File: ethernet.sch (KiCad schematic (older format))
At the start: 37 parts, among them J2 08B0-1X1T-36-F, U6 DP83848JSQ_NOPB, Y1 ABM8G-25.000MHZ-18-D2Y-T

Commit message: Clean FTDI
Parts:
- removed C117, C118, C119, C129: C_100n_0402_6V3, lpddr4-test-board-footprints:0402-cap, symbol lpddr4-test-board:C_100n_0402_6V3
- removed C127: C_1u_0402, lpddr4-test-board-footprints:0402-cap, symbol lpddr4-test-board:C_1u_0402
- removed R81: R_0R_0402, lpddr4-test-board-footprints:0402-res, symbol lpddr4-test-board:R_0R_0402
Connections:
- net at U6.27 (X2): now also C132.1, Y1.1
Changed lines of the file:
@@
-$EndComp
-$Comp
-L lpddr4-test-board:C_1u_0402 C127
-U 1 1 5F9F438B
-P 12025 4100
-F 0 "C127" H 12050 4200 60  0000 L CNN
-F 1 "C_1u_0402" H 12025 3950 60  0001 C CNN
-F 2 "lpddr4-test-board-footprints:0402-cap" H 12225 4300 60  0001 L CNN
-F 3 "" H 12025 4100 50  0001 C CNN
-F 4 "TDK" H 12225 4500 60  0001 L CNN "Manufacturer"
-F 5 "C1005X6S1A105K050BC" H 12225 4400 60  0001 L CNN "MPN"
-F 6 "1u" H 12050 4000 50  0000 L CNN "Val"
-	1    12025 4100
-	1    0    0    -1
-$EndComp
-$Comp
-L lpddr4-test-board:C_100n_0402_6V3 C129
-U 1 1 5F9F4394
-P 12325 4100
-F 0 "C129" H 12350 4200 60  0000 L CNN
-F 1 "C_100n_0402_6V3" H 12325 3950 60  0001 C CNN
-F 2 "lpddr4-test-board-footprints:0402-cap" H 12525 4300 60  0001 L CNN
-F 3 "" H 12325 4100 50  0001 C CNN
-F 4 "Walsin" H 12525 4500 60  0001 L CNN "Manufacturer"
-F 5 "0402X104K6R3CT" H 12525 4400 60  0001 L CNN "MPN"
-F 6 "100n" H 12350 4000 50  0000 L CNN "Val"
-	1    12325 4100
-	1    0    0    -1
 $EndComp
 $Comp
@@
 Text GLabel 11200 7000 2    50   Input ~ 0
 ETH_MDC
-$Comp
-L lpddr4-test-board:R_0R_0402 R81
-U 1 1 5FABAF2E
-P 11225 6700
-F 0 "R81" H 11025 6750 60  0000 C CNN
-F 1 "R_0R_0402" H 11225 6550 60  0001 C CNN
-F 2 "lpddr4-test-board-footprints:0402-res" H 11425 6900 60  0001 L CNN
-F 3 "" H 11225 6700 50  0001 C CNN
-F 4 "PANASONIC" H 11425 7100 60  0001 L CNN "Manufacturer"
-F 5 "ERJ2GE0R00X" H 11425 7000 60  0001 L CNN "MPN"
-F 6 "0R" H 11400 6650 50  0000 C CNN "Val"
-	1    11225 6700
-	1    0    0    -1
-$EndComp
-Wire Wire Line
-	10875 6700 11075 6700
-Wire Wire Line
-	11375 6700 13275 6700
 Wire Wire Line
 	13275 6700 13275 6850
@@
 Wire Wire Line
 	4500 5350 4300 5350
-$Comp
-L lpddr4-test-board:C_100n_0402_6V3 C117
-U 1 1 5FAAC848
-P 2925 4225
-F 0 "C117" H 2950 4325 60  0000 L CNN
-F 1 "C_100n_0402_6V3" H 2925 4075 60  0001 C CNN
-F 2 "lpddr4-test-board-footprints:0402-cap" H 3125 4425 60  0001 L CNN
-F 3 "" H 2925 4225 50  0001 C CNN
-F 4 "Walsin" H 3125 4625 60  0001 L CNN "Manufacturer"
-F 5 "0402X104K6R3CT" H 3125 4525 60  0001 L CNN "MPN"
-F 6 "100n" H 2950 4125 50  0000 L CNN "Val"
-	1    2925 4225
-	1    0    0    -1
-$EndComp
-$Comp
-L lpddr4-test-board:GND #PWR0137
-U 1 1 5FAAD2AA
-P 2925 4375
-F 0 "#PWR0137" H 2925 4125 50  0001 C CNN
-F 1 "GND" H 2930 4202 50  0000 C CNN
-F 2 "" H 2925 4375 50  0001 C CNN
-F 3 "" H 2925 4375 50  0001 C CNN
-	1    2925 4375
-	1    0    0    -1
-$EndComp
-Text GLabel 2925 4075 1    50   Input ~ 0
-ETH3V3
-$Comp
-L lpddr4-test-board:C_100n_0402_6V3 C118
-U 1 1 5FAAE999
-P 3325 4225
-F 0 "C118" H 3350 4325 60  0000 L CNN
-F 1 "C_100n_0402_6V3" H 3325 4075 60  0001 C CNN
-F 2 "lpddr4-test-board-footprints:0402-cap" H 3525 4425 60  0001 L CNN
-F 3 "" H 3325 4225 50  0001 C CNN
-F 4 "Walsin" H 3525 4625 60  0001 L CNN "Manufacturer"
-F 5 "0402X104K6R3CT" H 3525 4525 60  0001 L CNN "MPN"
-F 6 "100n" H 3350 4125 50  0000 L CNN "Val"
-	1    3325 4225
-	1    0    0    -1
-$EndComp
-$Comp
-L lpddr4-test-board:GND #PWR0138
-U 1 1 5FAAE99F
-P 3325 4375
-F 0 "#PWR0138" H 3325 4125 50  0001 C CNN
-F 1 "GND" H 3330 4202 50  0000 C CNN
-F 2 "" H 3325 4375 50  0001 C CNN
-F 3 "" H 3325 4375 50  0001 C CNN
-	1    3325 4375
-	1    0    0    -1
-$EndComp
-Text GLabel 3325 4075 1    50   Input ~ 0
-ETH3V3
-$Comp
-L lpddr4-test-board:C_100n_0402_6V3 C119
-U 1 1 5FAB6EB3
-P 3725 4225
-F 0 "C119" H 3775 4325 60  0000 L CNN
-F 1 "C_100n_0402_6V3" H 3725 4075 60  0001 C CNN
-F 2 "lpddr4-test-board-footprints:0402-cap" H 3925 4425 60  0001 L CNN
-F 3 "" H 3725 4225 50  0001 C CNN
-F 4 "Walsin" H 3925 4625 60  0001 L CNN "Manufacturer"
-F 5 "0402X104K6R3CT" H 3925 4525 60  0001 L CNN "MPN"
-F 6 "100n" H 3750 4125 50  0000 L CNN "Val"
-	1    3725 4225
-	1    0    0    -1
-$EndComp
-$Comp
-L lpddr4-test-board:GND #PWR0139
-U 1 1 5FAB6EB9
-P 3725 4375
-F 0 "#PWR0139" H 3725 4125 50  0001 C CNN
-F 1 "GND" H 3730 4202 50  0000 C CNN
-F 2 "" H 3725 4375 50  0001 C CNN
-F 3 "" H 3725 4375 50  0001 C CNN
-	1    3725 4375
-	1    0    0    -1
-$EndComp
-Text GLabel 3725 4075 1    50   Input ~ 0
-ETH3V3
-$Comp
-L lpddr4-test-board:C_100n_0402_6V3 C120
-U 1 1 5FAB6EC3
-P 4125 4225
-F 0 "C120" H 4175 4325 60  0000 L CNN
-F 1 "C_100n_0402_6V3" H 4125 4075 60  0001 C CNN
-F 2 "lpddr4-test-board-footprints:0402-cap" H 4325 4425 60  0001 L CNN
-F 3 "" H 4125 4225 50  0001 C CNN
-F 4 "Walsin" H 4325 4625 60  0001 L CNN "Manufacturer"
-F 5 "0402X104K6R3CT" H 4325 4525 60  0001 L CNN "MPN"
-F 6 "100n" H 4150 4125 50  0000 L CNN "Val"
-	1    4125 4225
-	1    0    0    -1
-$EndComp
-$Comp
-L lpddr4-test-board:GND #PWR0140
-U 1 1 5FAB6EC9
-P 4125 4375
-F 0 "#PWR0140" H 4125 4125 50  0001 C CNN
-F 1 "GND" H 4130 4202 50  0000 C CNN
-F 2 "" H 4125 4375 50  0001 C CNN
-F 3 "" H 4125 4375 50  0001 C CNN
-	1    4125 4375
-	1    0    0    -1
-$EndComp
-Text GLabel 4125 4075 1    50   Input ~ 0
-ETH3V3
 Wire Wire Line
 	3850 6500 3950 6500
@@
 L lpddr4-test-board:GND #PWR0143
 U 1 1 5FB2A11F
-P 12325 4450
-F 0 "#PWR0143" H 12325 4200 50  0001 C CNN
-F 1 "GND" H 12330 4277 50  0000 C CNN
-F 2 "" H 12325 4450 50  0001 C CNN
-F 3 "" H 12325 4450 50  0001 C CNN
-	1    12325 4450
+P 11725 4350
+F 0 "#PWR0143" H 11725 4100 50  0001 C CNN
+F 1 "GND" H 11730 4177 50  0000 C CNN
+F 2 "" H 11725 4350 50  0001 C CNN
+F 3 "" H 11725 4350 50  0001 C CNN
+	1    11725 4350
 	1    0    0    -1
 $EndComp
@@
 	11725 4250 11725 4350
 Wire Wire Line
-	11725 4350 12025 4350
-Wire Wire Line
-	12325 4350 12325 4450
-Wire Wire Line
-	12325 4350 12325 4250
-Connection ~ 12325 4350
-Wire Wire Line
-	12025 4250 12025 4350
-Connection ~ 12025 4350
-Wire Wire Line
-	12025 4350 12325 4350
-Wire Wire Line
 	11725 3950 11725 3850
-Wire Wire Line
-	11725 3850 12025 3850
-Wire Wire Line
-	12325 3850 12325 3950
-Wire Wire Line
-	12025 3950 12025 3850
-Connection ~ 12025 3850
-Wire Wire Line
-	12025 3850 12325 3850
-Text GLabel 12025 3700 1    50   Input ~ 0
+Connection ~ 11725 3850
+Text GLabel 11725 3725 1    50   Input ~ 0
 ETH3V3
 Wire Wire Line
 	11175 4700 11175 3850
 Wire Wire Line
-	12025 3700 12025 3850
+	11725 3725 11725 3850
 Text GLabel 12775 4600 1    50   Input ~ 0
 VCC3V3
@@
 Wire Wire Line
 	11350 3850 11725 3850
-Connection ~ 11725 3850
 Wire Wire Line
 	11175 3850 11350 3850
@@
 Text Notes 8750 3100 0    118  ~ 24
 Ethernet transceiver
+Wire Wire Line
+	10875 6700 13275 6700
+Text GLabel 4125 4075 1    50   Input ~ 0
+ETH3V3
+$Comp
+L lpddr4-test-board:GND #PWR0140
+U 1 1 5FAB6EC9
+P 4125 4375
+F 0 "#PWR0140" H 4125 4125 50  0001 C CNN
+F 1 "GND" H 4130 4202 50  0000 C CNN
+F 2 "" H 4125 4375 50  0001 C CNN
+F 3 "" H 4125 4375 50  0001 C CNN
+	1    4125 4375
+	1    0    0    -1
+$EndComp
+$Comp
+L lpddr4-test-board:C_100n_0402_6V3 C120
+U 1 1 5FAB6EC3
+P 4125 4225
+F 0 "C120" H 4175 4325 60  0000 L CNN
+F 1 "C_100n_0402_6V3" H 4125 4075 60  0001 C CNN
+F 2 "lpddr4-test-board-footprints:0402-cap" H 4325 4425 60  0001 L CNN
+F 3 "" H 4125 4225 50  0001 C CNN
+F 4 "Walsin" H 4325 4625 60  0001 L CNN "Manufacturer"
+F 5 "0402X104K6R3CT" H 4325 4525 60  0001 L CNN "MPN"
+F 6 "100n" H 4150 4125 50  0000 L CNN "Val"
+	1    4125 4225
+	1    0    0    -1
+$EndComp
 $EndSCHEMATC

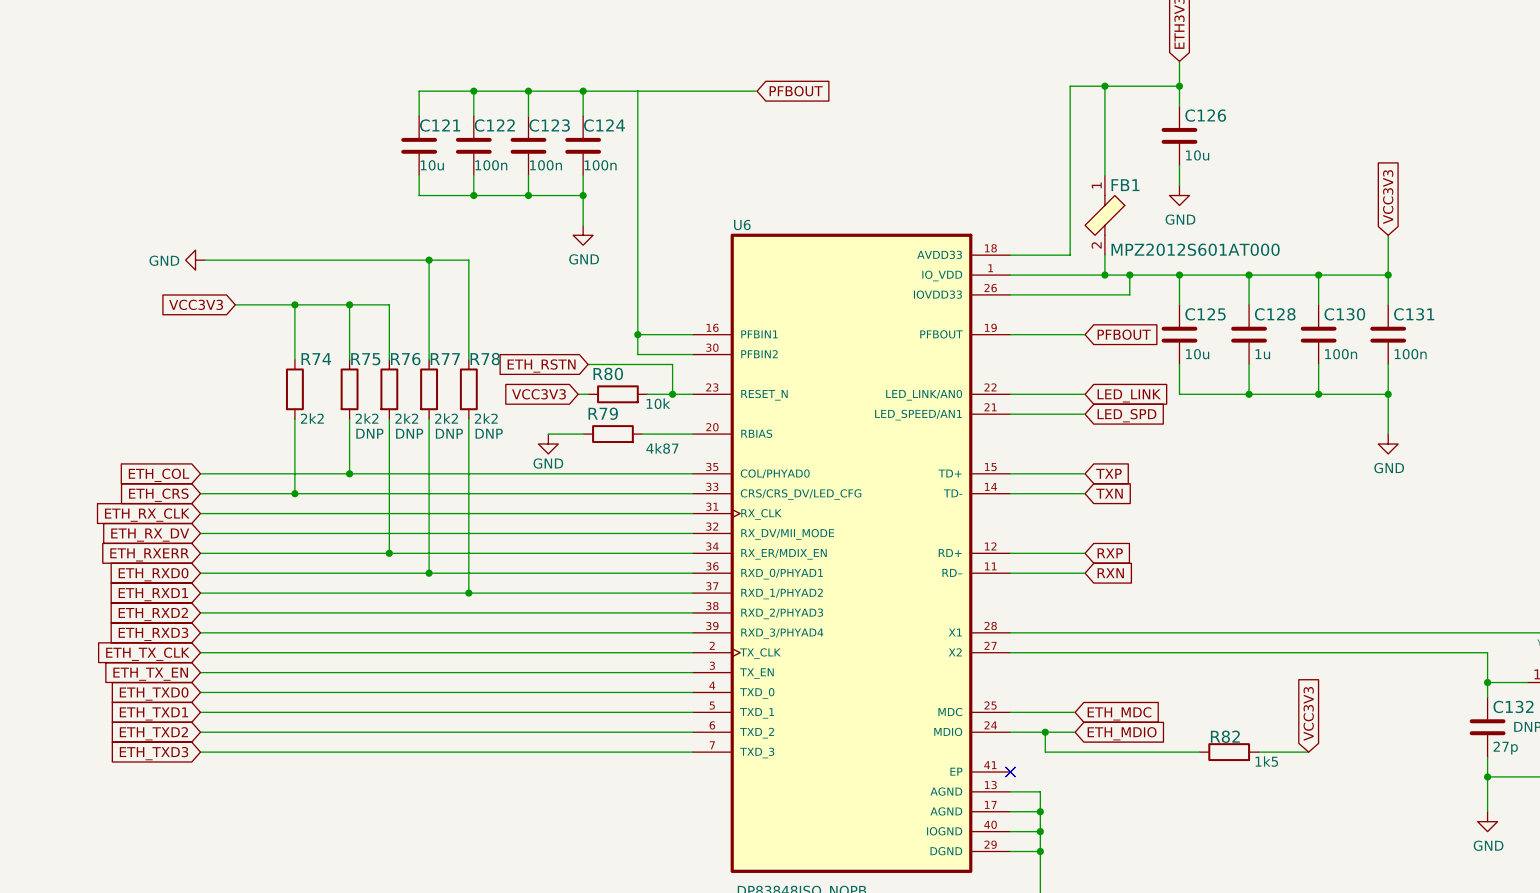
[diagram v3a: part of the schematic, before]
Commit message: Replace VCC3V3 with 3V3_SYS
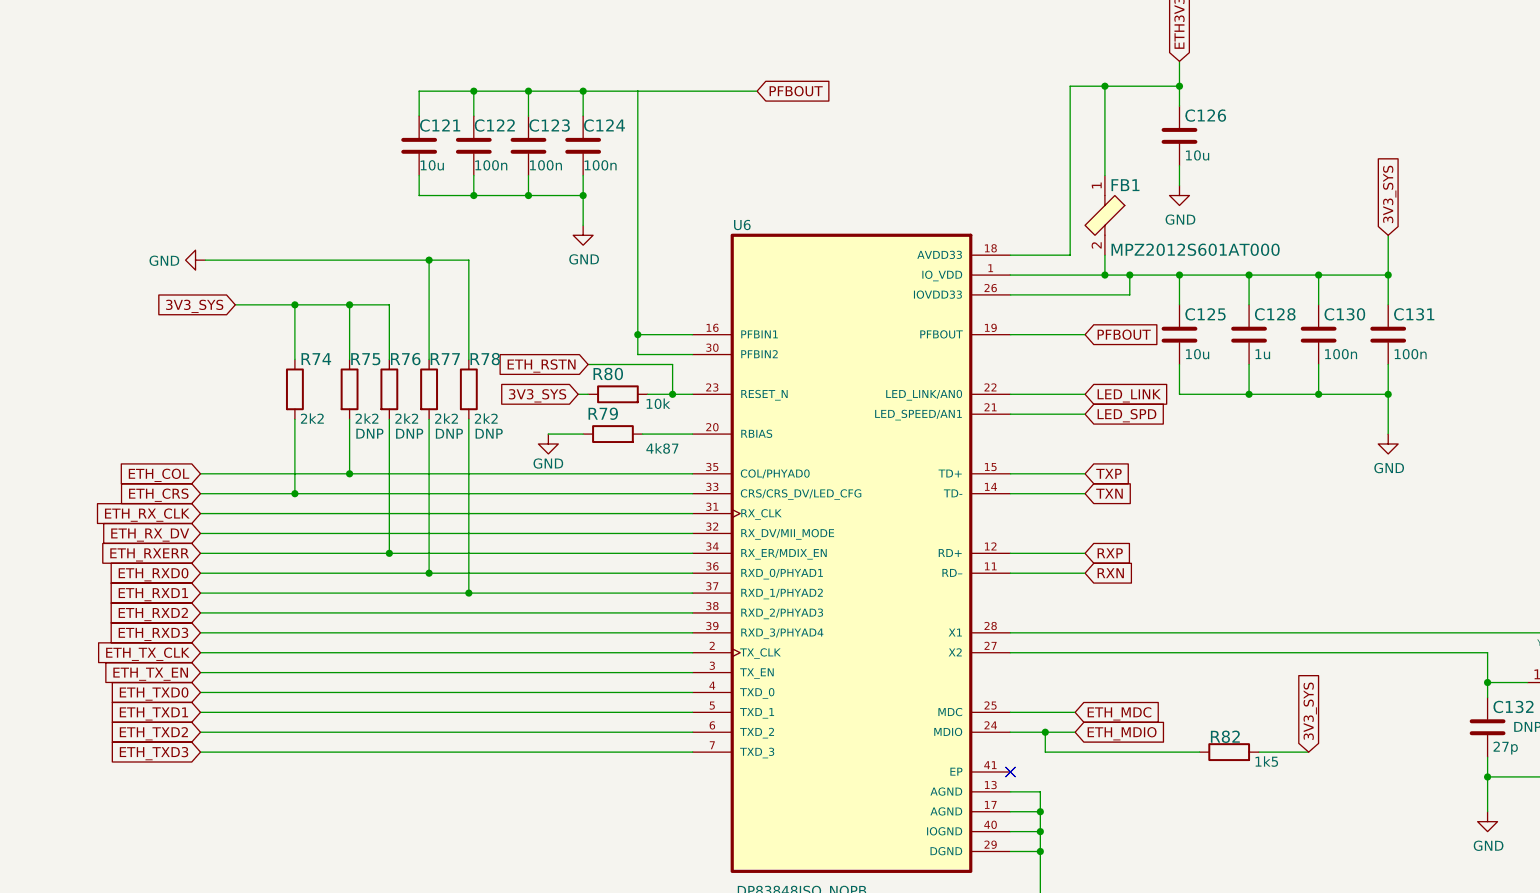
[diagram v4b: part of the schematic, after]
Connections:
- net VCC3V3 renamed 3V3_SYS
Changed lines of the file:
@@
 	11725 3725 11725 3850
 Text GLabel 12775 4600 1    50   Input ~ 0
-VCC3V3
+3V3_SYS
 Wire Wire Line
 	12775 4600 12775 4800
@@
 Connection ~ 12775 5400
 Text GLabel 12375 7200 1    50   Input ~ 0
-VCC3V3
+3V3_SYS
 Wire Wire Line
 	12125 7200 12375 7200
@@
 	11025 7700 11025 8000
 Text GLabel 6975 4950 0    50   Input ~ 0
-VCC3V3
+3V3_SYS
 Wire Wire Line
 	6975 4950 7275 4950
@@
 $EndComp
 Text GLabel 8700 5400 0    50   Input ~ 0
-VCC3V3
+3V3_SYS
 Wire Wire Line
 	8750 5400 8700 5400
